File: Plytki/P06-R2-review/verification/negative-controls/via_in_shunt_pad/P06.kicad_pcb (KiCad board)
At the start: 2 copper layers, 106.5 x 100 mm, 81 parts, among them J3 ISERIES, J4 SW1 A, J5 SW1 B, U1 INA240A2, U10 MCP1525-I/TO, U2 MCP6022-I/P, U3 MCP3201-BI/P, U4 MCP1702-3302E/TO, U5 74LVC125AD, U6 74LVC125AD, U7 SN74HC08N, U8 MCP120-300DI/TO, U9 MCP120-450DI/TO

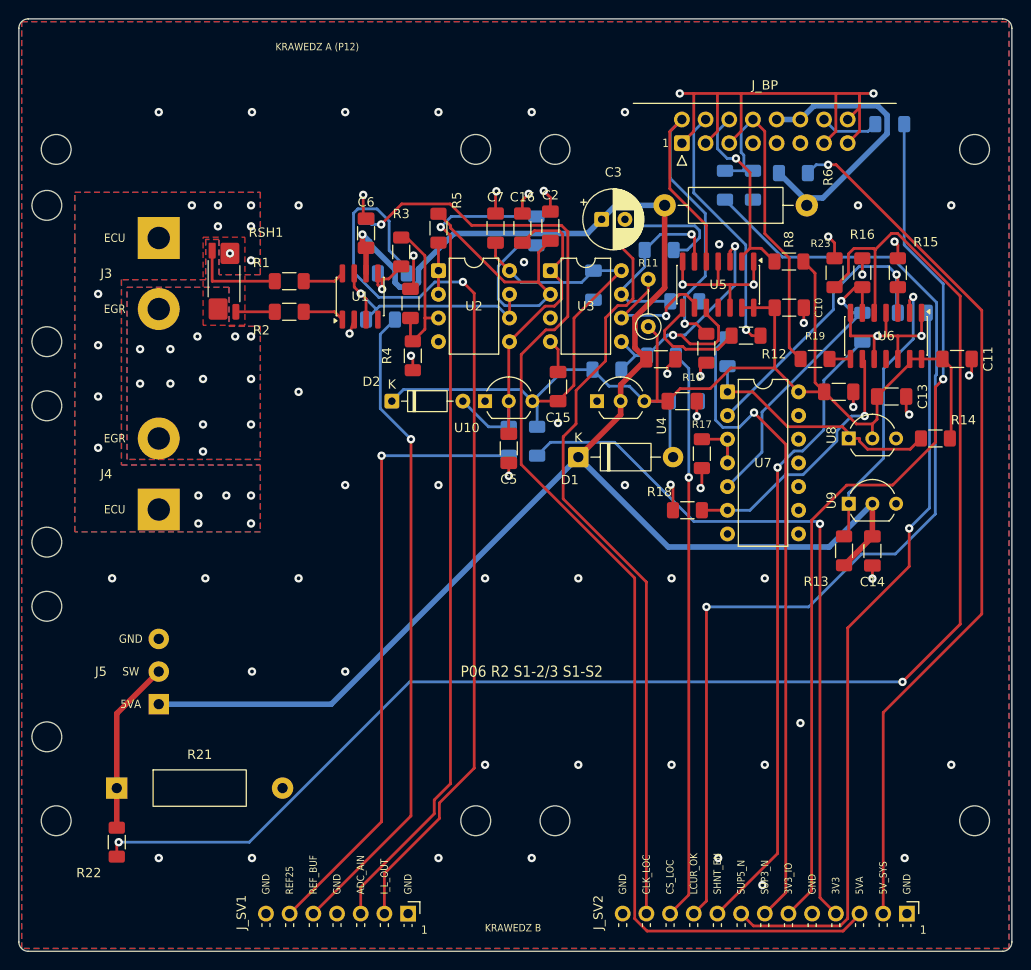
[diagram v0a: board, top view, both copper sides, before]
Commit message: P06 R2: poprawki po niezależnej recenzji PCB (2.10) — nadruk 1,0/0,15 mm, masa pod U2/U3, powrót masy odsprzęgania
- F1: wszystkie napisy nadruku >= 1,0 mm / 0,15 mm (minimum JLCPCB), minimum w regułach DRC
- F2/F3: wnętrza U2/U3, pas między nimi i strefa pod dolnymi pinami U2 bez obcej miedzi (strefy routera);
  kondensatory odsprzęgające rozmieszczane według padu zasilania i padu masy; C2 pod U3 przy IN+/IN-;
  D1 niżej; R30 przy U9.2; R10 pod U5; przelotki GND przy kondensatorach (stitch.py --targeted) i
  tor masy z planera dla C12 (complete_routes.py --ties)
- nowa kontrola: droga po miedzi GND kondensator -> pin GND układu (src/gndpath.py); odrzucanie prób
  trasowania z kolizjami miedzi
- DRC 0/0/0 (3 x lib_footprint_mismatch przyjęte), kontrole PCB 34/34, próby ujemne 37/37

Co-Authored-By: Claude Opus 5.5 <noreply@anthropic.com>
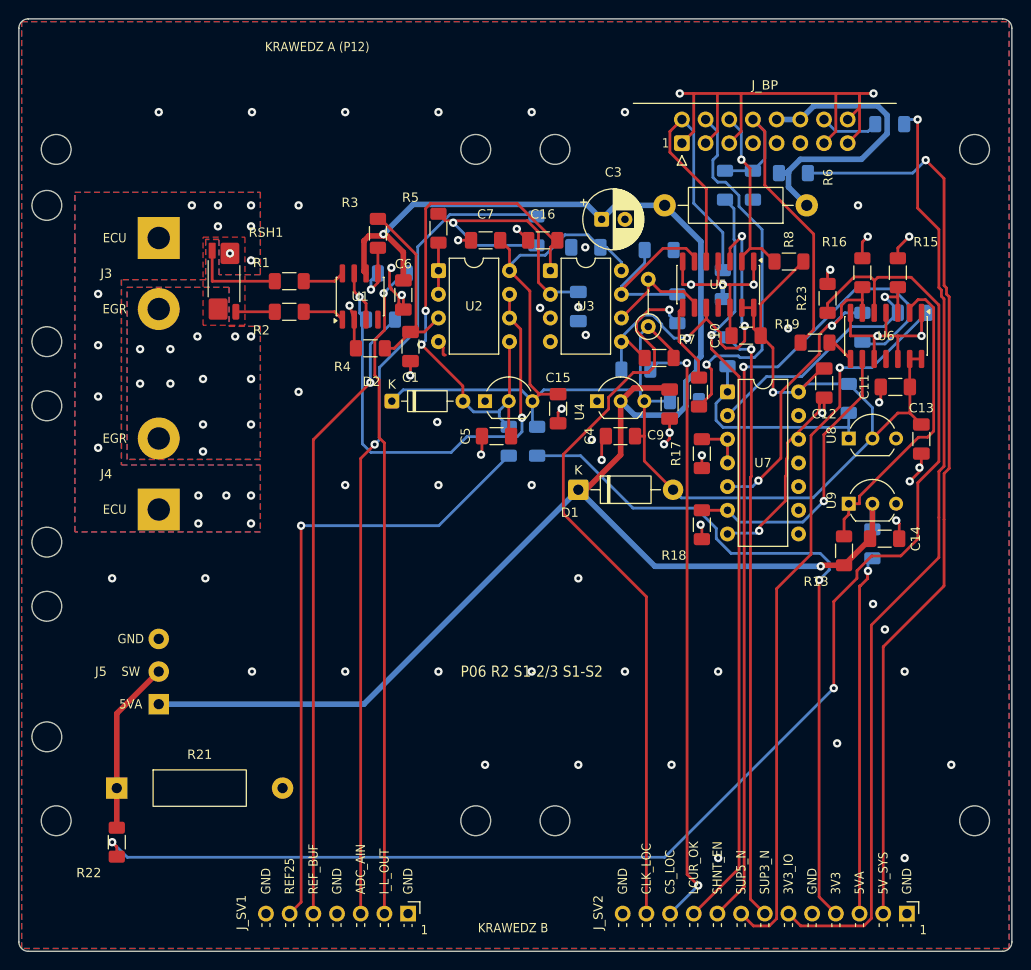
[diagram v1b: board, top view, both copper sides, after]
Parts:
- C2, R10, R14: moved to B.Cu
- R7: moved to F.Cu
- moved R30 63.7 mm to (91.5, 56.3), turned to -90 degrees
- moved R14 10.2 mm to (89.0, 40.7), turned to -90 degrees
- moved C2 9.13 mm to (60.0, 30.9), turned to -90 degrees
- moved R12 7.88 mm to (72.9, 40.0), turned to -90 degrees
- moved C6 7.74 mm to (41.2, 29.6), turned to -90 degrees
- moved C4 7.61 mm to (64.5, 44.8), turned to 180 degrees
- moved C11 7.27 mm to (94.0, 39.5), turned to 180 degrees
- moved R10 7.05 mm to (75.5, 28.5)
- moved R38 6.59 mm to (70.6, 31.1), turned to -90 degrees
- moved R9 6.15 mm to (68.7, 24.8)
- moved R7 5.74 mm to (68.7, 36.4), turned to 180 degrees
- moved C13 5.56 mm to (96.8, 45.1), turned to -90 degrees
- moved C10 5.51 mm to (78.0, 34.0), turned to 180 degrees
- moved C9 4.90 mm to (69.8, 41.3), turned to -90 degrees
- moved C1 4.63 mm to (42.0, 35.1), turned to -90 degrees
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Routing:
- net /SERWIS/SRV_5VA_P06: track 130.9 -> 38.9 mm
- net /SERWIS/SRV_I_L_OUT: track 103.0 -> 70.8 mm
- net /SERWIS/SRV_LOGGER_CURRENT_OK: track 112.1 -> 81.3 mm
- net REF_BUF: track 26.9 -> 55.4 mm, vias 1 -> 2
- net GND: track 138.0 -> 162.9 mm, vias 65 -> 67
- net REF25: track 39.2 -> 60.9 mm, vias 0 -> 2
- net /SERWIS/SRV_SHUNT_ENABLED: track 68.3 -> 89.5 mm
- net /SERWIS/SRV_CLK_LOCAL: track 93.6 -> 78.8 mm
- net 5VA_P06: track 178.2 -> 191.4 mm, vias 1 -> 2
- net ADC_DOUTA: track 27.2 -> 40.2 mm
- net 3V3_P06: track 163.4 -> 174.6 mm, vias 0 -> 1
- net ADC_SCLK: track 45.1 -> 35.4 mm, vias 1 -> 0
- net /READY/SW_SENSE: track 163.5 -> 154.0 mm
- net CS_LOCAL_N: track 33.6 -> 41.0 mm, vias 2 -> 3
- net /SERWIS/SRV_SUP3_N: track 70.6 -> 64.3 mm
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
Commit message: P06 R2: szprychy 4 x 2 mm na polach J3/J4, C17 100 nF na 5VA przy J5 (decyzje użytkownika 2.10)
- route_critical.py: pola przewodów J3/J4 na szprychach (wylewki mocy: szprycha 2 mm, szczelina 0,5 mm), RSH1 pełne;
  wylewka ECU_P1 pod J4.1 dłuższa o 2,45 mm (czwarta szprycha)
- schemat: C17 100 nF 1206 5VA_P06 / GND przy J5 (uwaga F7 recenzji); C1 zostaje X7R
- trasowanie zatwierdzonej wersji odtworzone, planer dołożył połączenia C17 (szerokość klasy PWR 0,6 mm w planerze)
- run_layout.py: return_check.py odrzuca próby z za długim powrotem masy odsprzęgania
- kontrole PCB 34/34 (siła: szprychy i korytarz liczone od wypełnienia wokół pól), próby ujemne 37/37

Co-Authored-By: Claude Opus 5.5 <noreply@anthropic.com>
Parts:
- added C17: 100n, Capacitor_SMD:C_1206_3216Metric_Pad1.33x1.80mm_HandSolder, F.Cu at (18.5, 69.9)
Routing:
- net 5VA_P06: track 191.4 -> 210.8 mm, vias 2 -> 3
- net GND: vias 67 -> 68
